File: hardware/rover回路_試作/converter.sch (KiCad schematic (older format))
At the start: 0 parts

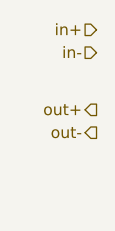
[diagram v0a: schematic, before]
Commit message: rover回路最終版v1.0 降圧回路に関してのみ未記載
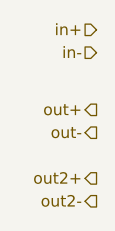
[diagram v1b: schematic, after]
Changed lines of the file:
@@
 $Descr A4 11693 8268
 encoding utf-8
-Sheet 5 7
+Sheet 4 8
 Title ""
 Date ""
@@
 Text HLabel 6500 4000 0    50   Output ~ 0
 out-
+Text HLabel 6500 4200 0    50   Output ~ 0
+out2+
+Text HLabel 6500 4300 0    50   Output ~ 0
+out2-
 $EndSCHEMATC

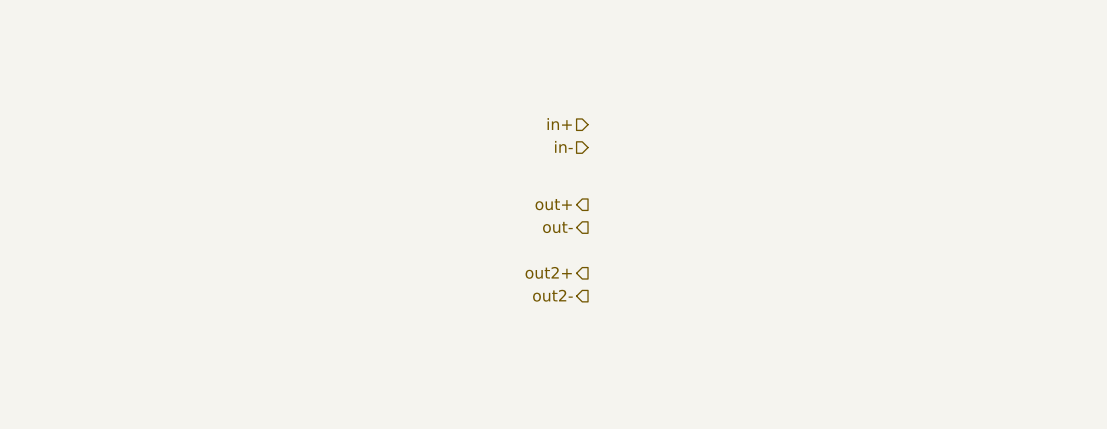
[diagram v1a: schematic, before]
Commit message: DCDC回路図追加
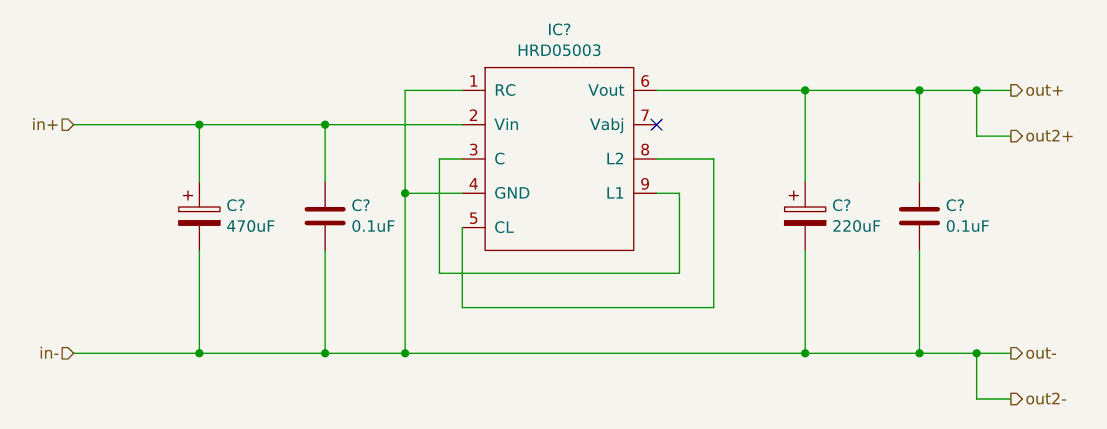
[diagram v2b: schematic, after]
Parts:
- added C? (x2): 0.1uF, symbol Device:C
- added C?: 470uF, symbol Device:CP
- added C?: 220uF, symbol Device:CP
- added IC?: HRD05003, symbol New_Library:HRD05003
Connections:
- net in+: now also C?.1, C?.1, IC?.2 (Vin)
- net in-: now also C?.2, C?.2, C?.2, C?.2, IC?.1 (RC), IC?.4 (GND)
- net out+: now also C?.1, C?.1, IC?.6 (Vout)
- new net: IC?.3 (C), IC?.9 (L1)
- new net: IC?.5 (CL), IC?.8 (L2)
- no-connect marks 0 -> 1
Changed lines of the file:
@@
 $Descr A4 11693 8268
 encoding utf-8
-Sheet 4 8
+Sheet 3 8
 Title ""
 Date ""
@@
 Comment4 ""
 $EndDescr
-Text HLabel 6500 3550 0    50   Input ~ 0
+Text HLabel 4250 3550 0    50   Input ~ 0
 in+
-Text HLabel 6500 3650 0    50   Input ~ 0
+Text HLabel 4250 4550 0    50   Input ~ 0
 in-
-Text HLabel 6500 3900 0    50   Output ~ 0
+Text HLabel 8350 3400 2    50   Output ~ 0
 out+
-Text HLabel 6500 4000 0    50   Output ~ 0
+Text HLabel 8350 4550 2    50   Output ~ 0
 out-
-Text HLabel 6500 4200 0    50   Output ~ 0
+Text HLabel 8350 3600 2    50   Output ~ 0
 out2+
-Text HLabel 6500 4300 0    50   Output ~ 0
+Text HLabel 8350 4750 2    50   Output ~ 0
 out2-
+$Comp
+L New_Library:HRD05003 IC?
+U 1 1 61FFECDD
+P 6250 3100
+F 0 "IC?" H 6375 3065 50  0000 C CNN
+F 1 "HRD05003" H 6375 2974 50  0000 C CNN
+F 2 "" H 6250 3000 50  0001 C CNN
+F 3 "" H 6250 3000 50  0001 C CNN
+	1    6250 3100
+	1    0    0    -1
+$EndComp
+Wire Wire Line
+	5950 3550 5350 3550
+Wire Wire Line
+	4250 4550 4800 4550
+$Comp
+L Device:C C?
+U 1 1 620015B3
+P 5350 3950
+F 0 "C?" H 5465 3996 50  0000 L CNN
+F 1 "0.1uF" H 5465 3905 50  0000 L CNN
+F 2 "" H 5388 3800 50  0001 C CNN
+F 3 "~" H 5350 3950 50  0001 C CNN
+	1    5350 3950
+	1    0    0    -1
+$EndComp
+$Comp
+L Device:C C?
+U 1 1 620018BA
+P 7950 3950
+F 0 "C?" H 8065 3996 50  0000 L CNN
+F 1 "0.1uF" H 8065 3905 50  0000 L CNN
+F 2 "" H 7988 3800 50  0001 C CNN
+F 3 "~" H 7950 3950 50  0001 C CNN
+	1    7950 3950
+	1    0    0    -1
+$EndComp
+$Comp
+L Device:CP C?
+U 1 1 6200219E
+P 4800 3950
+F 0 "C?" H 4918 3996 50  0000 L CNN
+F 1 "470uF" H 4918 3905 50  0000 L CNN
+F 2 "" H 4838 3800 50  0001 C CNN
+F 3 "~" H 4800 3950 50  0001 C CNN
+	1    4800 3950
+	1    0    0    -1
+$EndComp
+$Comp
+L Device:CP C?
+U 1 1 620027A3
+P 7450 3950
+F 0 "C?" H 7568 3996 50  0000 L CNN
+F 1 "220uF" H 7568 3905 50  0000 L CNN
+F 2 "" H 7488 3800 50  0001 C CNN
+F 3 "~" H 7450 3950 50  0001 C CNN
+	1    7450 3950
+	1    0    0    -1
+$EndComp
+Wire Wire Line
+	4800 3550 4800 3800
+Connection ~ 4800 3550
+Wire Wire Line
+	4800 3550 4250 3550
+Wire Wire Line
+	4800 4100 4800 4550
+Connection ~ 4800 4550
+Wire Wire Line
+	4800 4550 5350 4550
+Wire Wire Line
+	5350 4550 5350 4100
+Connection ~ 5350 4550
+Wire Wire Line
+	5350 4550 5700 4550
+Connection ~ 5350 3550
+Wire Wire Line
+	5350 3550 4800 3550
+Wire Wire Line
+	5950 3400 5700 3400
+Wire Wire Line
+	5700 3400 5700 3850
+Connection ~ 5700 4550
+Wire Wire Line
+	5950 3850 5700 3850
+Connection ~ 5700 3850
+Wire Wire Line
+	5700 3850 5700 4550
+Wire Wire Line
+	5950 4000 5950 4350
+Wire Wire Line
+	5950 4350 7050 4350
+Wire Wire Line
+	7050 4350 7050 3700
+Wire Wire Line
+	7050 3700 6800 3700
+Wire Wire Line
+	5950 3700 5850 3700
+Wire Wire Line
+	5850 3700 5850 4200
+Wire Wire Line
+	5850 4200 6900 4200
+Wire Wire Line
+	6900 4200 6900 3850
+Wire Wire Line
+	6900 3850 6800 3850
+NoConn ~ 6800 3550
+Wire Wire Line
+	5700 4550 7450 4550
+Wire Wire Line
+	6800 3400 7450 3400
+Wire Wire Line
+	8200 3400 8200 3600
+Wire Wire Line
+	8200 3600 8350 3600
+Connection ~ 8200 3400
+Wire Wire Line
+	8200 3400 8350 3400
+Wire Wire Line
+	8200 4750 8350 4750
+Wire Wire Line
+	8200 4550 8200 4750
+Connection ~ 8200 4550
+Wire Wire Line
+	8200 4550 8350 4550
+Wire Wire Line
+	5350 3550 5350 3800
+Wire Wire Line
+	7450 3800 7450 3400
+Connection ~ 7450 3400
+Wire Wire Line
+	7450 3400 7950 3400
+Connection ~ 7450 4550
+Wire Wire Line
+	7450 4550 7950 4550
+Wire Wire Line
+	7450 4100 7450 4550
+Connection ~ 7950 4550
+Wire Wire Line
+	7950 4550 8200 4550
+Wire Wire Line
+	7950 4100 7950 4550
+Wire Wire Line
+	7950 3800 7950 3400
+Connection ~ 7950 3400
+Wire Wire Line
+	7950 3400 8200 3400
 $EndSCHEMATC
